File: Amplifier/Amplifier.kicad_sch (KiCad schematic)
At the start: 55 parts, among them J7 Conn_01x14_MountingPin, Q3 2N7002, U13 AD40xxBRMZ, U14 LP5907MFX-1.8, U16 LTC6268xS8, U2 LMP7721, U6 ADA4940-1xCP

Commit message: commiting pcb changes
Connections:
- net VDDA: now also J7.10 (Pin_10); no longer J7.12 (Pin_12)
- net VSSA: now also J7.12 (Pin_12); no longer J7.10 (Pin_10)
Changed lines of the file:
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@@
 	(symbol
 		(lib_id "power:VDDA")
-		(at 49.53 111.76 90)
+		(at 49.53 106.68 90)
 		(mirror x)
 		(unit 1)
@@
 		(fields_autoplaced yes)
 		(property "Reference" "#PWR024"
-			(at 53.34 111.76 0)
+			(at 53.34 106.68 0)
 			(hide yes)
 			(show_name no)
@@
 		)
 		(property "Value" "VDDA"
-			(at 46.355 111.7601 90)
+			(at 46.355 106.6801 90)
 			(show_name no)
 			(do_not_autoplace no)
@@
 		)
 		(property "Footprint" ""
-			(at 49.53 111.76 0)
+			(at 49.53 106.68 0)
 			(hide yes)
 			(show_name no)
@@
 		)
 		(property "Datasheet" ""
-			(at 49.53 111.76 0)
+			(at 49.53 106.68 0)
 			(hide yes)
 			(show_name no)
@@
 		)
 		(property "Description" "Power symbol creates a global label with name \"VDDA\""
-			(at 49.53 111.76 0)
+			(at 49.53 106.68 0)
 			(hide yes)
 			(show_name no)
@@
 	(symbol
 		(lib_id "power:VSSA")
-		(at 49.53 106.68 90)
+		(at 49.53 111.76 90)
 		(unit 1)
 		(body_style 1)
@@
 		(dnp no)
 		(property "Reference" "#PWR022"
-			(at 53.34 106.68 0)
+			(at 53.34 111.76 0)
 			(hide yes)
 			(show_name no)
@@
 		)
 		(property "Value" "VSSA"
-			(at 46.228 106.68 90)
+			(at 46.228 111.76 90)
 			(show_name no)
 			(do_not_autoplace no)
@@
 		)
 		(property "Footprint" ""
-			(at 49.53 106.68 0)
+			(at 49.53 111.76 0)
 			(hide yes)
 			(show_name no)
@@
 		)
 		(property "Datasheet" ""
-			(at 49.53 106.68 0)
+			(at 49.53 111.76 0)
 			(hide yes)
 			(show_name no)
@@
 		)
 		(property "Description" "Power symbol creates a global label with name \"VSSA\""
-			(at 49.53 106.68 0)
-			(hide yes)
-			(show_name no)
+			(at 49.53 111.76 0)
+			(hide yes)
+			(show_name no)

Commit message: chore: prepare repository and documentation for open-source release
- Removed internal .agents scaffolding and updated .gitignore
- Added CONTRIBUTING.md with CAD, PCB, firmware, and PR guidelines
- Added CODE_OF_CONDUCT.md (Contributor Covenant v2.1)
- Added SECURITY.md with hardware safety and vulnerability disclosure policies
- Added CITATION.cff for academic and scientific publications
- Added Pump_firmware/README.md for STM32G431 subsystem
- Expanded BOM.md with mechanical, fluidic, PCB, and active electronics
- Updated README.md test badges, architecture, and documentation index
- Cleared hardcoded absolute developer paths in export_manager.py and KiCad files
- Fixed formatting in install.sh and metadata in package.json
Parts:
- removed NT5: NetTie_2, NetTie:NetTie-2_SMD_Pad0.5mm, symbol Device:NetTie_2
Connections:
- net Signal_AMP: no longer C9.1, R3.1, R45.1, U16.6
- new net Signal_Return: C9.1, R3.1, R45.1, U16.6
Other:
- moved on the sheet: C9, R5

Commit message: feat: Add Path 2 wideband TIA channel for 200nm pores
Co-authored-by: google-labs-jules[bot] <161369871+google-labs-jules[bot]@users.noreply.github.com>
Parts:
- J_POGO1: value PogoPin_SpringHeader_6Pin_Array -> PogoPin_SpringHeader_12Pin_Distributed; footprint footprints:PogoPin_Target_6Pin_Distributed -> footprints:PogoPin_SpringHeader_12Pin_Distributed; symbol MR1:PogoPin_SpringHeader_6Pin_Array -> MR1:PogoPin_SpringHeader_12Pin_Distributed
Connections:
- net >PORE_AMP: no longer J_POGO1.6 (WE_POS)
- net CE_GNDA: no longer J_POGO1.1 (CE_GNDA)
- net GNDA: no longer J_POGO1.3 (GNDA)
- net RE_TRANS: no longer J_POGO1.2 (RE_TRANS)
- net R_WEEP_LIM: no longer J_POGO1.5 (WS_CIS)
- net WS_CIS: no longer J_POGO1.4 (WEEP_SENSE)
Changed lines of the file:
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@@
 	)
 	(symbol
-		(lib_id "MR1:PogoPin_SpringHeader_6Pin_Array")
+		(lib_id "MR1:PogoPin_SpringHeader_12Pin_Distributed")
 		(at 46.99 30.48 0)
 		(unit 1)
@@
 			)
 		)
-		(property "Value" "PogoPin_SpringHeader_6Pin_Array"
+		(property "Value" "PogoPin_SpringHeader_12Pin_Distributed"
 			(at 58.42 31.7499 0)
 			(show_name no)
@@
 			)
 		)
-		(property "Footprint" "footprints:PogoPin_Target_6Pin_Distributed"
+		(property "Footprint" "footprints:PogoPin_SpringHeader_12Pin_Distributed"
 			(at 46.99 30.48 0)
 			(hide yes)
@@
 		(pin "6"
 		)
+		(pin "7")
+		(pin "8")
+		(pin "9")
+		(pin "10")
+		(pin "11")
+		(pin "12")
 		(instances
 			(project "Amplifier"
@@
 	(embedded_fonts no)
 )
+	(label "WS_CIS_WIDE" (at 40.64 125.0 180) (effects (font (size 1.27 1.27))))
+	(label "GUARD_WIDE" (at 40.64 130.0 180) (effects (font (size 1.27 1.27))))
+	(symbol (lib_id "Amplifier_Operational:OPA192") (at 100.0 125.0 0) (unit 1)
+		(property "Reference" "U17" (at 101.6 120.0 0) (effects (font (size 1.27 1.27))))
+		(property "Value" "OPA192" (at 101.6 122.5 0) (effects (font (size 1.27 1.27))))
+	)
+	(symbol (lib_id "Device:R") (at 100.0 115.0 90) (unit 1)
+		(property "Reference" "Rf2" (at 100.0 112.0 0) (effects (font (size 1.27 1.27))))
+		(property "Value" "100k" (at 100.0 118.0 0) (effects (font (size 1.27 1.27))))
+	)
+	(symbol (lib_id "Device:C") (at 100.0 110.0 90) (unit 1)
+		(property "Reference" "Cf2" (at 100.0 107.0 0) (effects (font (size 1.27 1.27))))
+		(property "Value" "15pF" (at 100.0 109.0 0) (effects (font (size 1.27 1.27))))
+	)
+	(wire (pts (xy 40.64 125.0) (xy 90.0 125.0)) (stroke (width 0) (type default)))
+	(wire (pts (xy 90.0 125.0) (xy 90.0 115.0)) (stroke (width 0) (type default)))
+	(wire (pts (xy 90.0 115.0) (xy 95.0 115.0)) (stroke (width 0) (type default)))
+	(wire (pts (xy 90.0 115.0) (xy 90.0 110.0)) (stroke (width 0) (type default)))
+	(wire (pts (xy 90.0 110.0) (xy 95.0 110.0)) (stroke (width 0) (type default)))
+	(wire (pts (xy 105.0 115.0) (xy 110.0 115.0)) (stroke (width 0) (type default)))
+	(wire (pts (xy 105.0 110.0) (xy 110.0 110.0)) (stroke (width 0) (type default)))
+	(wire (pts (xy 110.0 115.0) (xy 110.0 125.0)) (stroke (width 0) (type default)))
+	(wire (pts (xy 110.0 110.0) (xy 110.0 115.0)) (stroke (width 0) (type default)))
+	(wire (pts (xy 110.0 125.0) (xy 120.0 125.0)) (stroke (width 0) (type default)))
+	(label "Path2_OUT" (at 120.0 125.0 0) (effects (font (size 1.27 1.27))))

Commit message: lots of refinements.
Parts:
- removed J_POGO1: PogoPin_SpringHeader_12Pin_Distributed, footprints:PogoPin_SpringHeader_12Pin_Distributed, symbol MR1:PogoPin_SpringHeader_12Pin_Distributed
- added C14: 100nF, Capacitor_SMD:C_0805_2012Metric, symbol Device:C
- added C3: 15pF, Capacitor_SMD:C_0402_1005Metric, symbol Device:C
- added C34: 100nF, Capacitor_SMD:C_0402_1005Metric, symbol Device:C
- added FB1, FB2: HZ0402A152R-10, Inductor_SMD:L_0402_1005Metric, symbol Device:FerriteBead_Small
- added J_POGO2: PogoPin_SpringHeader_12Pin_Distributed, footprints:PogoPin_SpringHeader_12Pin_Distributed, symbol MR1:PogoPin_SpringHeader_12Pin_Distributed
- added NT6: NetTie_2, NetTie:NetTie-2_SMD_Pad0.5mm, symbol Device:NetTie_2
- added R10: 100k, Resistor_SMD:R_0402_1005Metric, symbol Device:R
- added R32, R33: 49.9, Resistor_SMD:R_0402_1005Metric, symbol Device:R_Small_US
- added R9: 1K, Resistor_SMD:R_0402_1005Metric, symbol Device:R
- added U5: OPA192IDR, footprints:SOIC-8_3.9x4.9mm_P1.27mm, symbol MR1:OPA192IDR
- R1: value 1M -> 1G
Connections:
- net +3V3: now also FB1.1, FB2.1; no longer C33.1, U13.10 (VIO), U14.1 (IN)
- net >PORE_AMP: now also J_POGO2.3 (>PORE)
- net CE_GNDA: now also J_POGO2.1 (CE_GNDA)
- net GND: no longer C11.2, J7.4 (Pin_4), U14.2 (GND)
- net GNDA: now also C11.2, U14.2 (GND), C14.2, C34.2, J_POGO2.11 (GNDA), J_POGO2.4 (GNDA), J_POGO2.8 (GNDA)
- net GUARD: now also J_POGO2.5 (GUARD), J_POGO2.7 (GUARD)
- net RE_TRANS: now also J_POGO2.2 (RE_TRANS), R9.2
- net R_WEEP_LIM: now also J_POGO2.12 (WEEP_SENSE)
- net Signal_Return: now also R32.2
- net VDDA: now also U5.7 (V+)
- net VSSA: now also U5.4 (V-)
- net Vbias: now also C14.1, NT6.2, R9.1, U5.3 (+)
- net WS_CIS: now also J_POGO2.6 (WS_CIS)
- new net: C3.1, R10.1, R32.1, U5.6
- new net: C34.1, FB2.2, U14.1 (IN)
- new net: J7.4 (Pin_4), R33.2
- new net +3.3VA: C33.1, FB1.2, U13.10 (VIO)
- new net GUARD_WIDE: J_POGO2.9 (GUARD_WIDE), NT6.1, U5.1 (NC), U5.5 (NC), U5.8 (NC)
- new net ROUTE_SEL: R33.1
- new net WS_CIS_WIDE: C3.2, J_POGO2.10 (WS_CIS_WIDE), R10.2, U5.2 (-)

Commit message: there's issues with the constrictic iterposer mating pad showing up
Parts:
- removed NT6: NetTie_2, NetTie:NetTie-2_SMD_Pad0.5mm, symbol Device:NetTie_2
- added C40, C42: 100nF, Capacitor_SMD:C_0402_1005Metric, symbol Device:C
- added J_PAD1: Concentric_Interposer_Mating_Pad, footprints:Concentric_Interposer_Mating_Pad, symbol MR1:Concentric_Interposer_Mating_Pad
- added U17: ADG1219BRMZ, footprints:MSOP-8_3x3mm_P0.65mm, symbol MR1:ADG1219BRMZ
- added unit 2 of U5
- U5: value OPA192IDR -> OPA2192IDR; symbol MR1:OPA192IDR -> MR1:OPA2192IDR; MPN OPA192IDR -> OPA2192IDR; Mouser PN 595-OPA192IDR -> 595-OPA2192IDR
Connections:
- net +3V3: now also U17.1 (EN)
- net >PORE_AMP: now also J_PAD1.1 (SIG)
- net GNDA: now also C40.2, C42.2, U17.3 (GND)
- net GUARD: now also J_PAD1.2 (GUARD)
- net GUARD_WIDE: now also U5.6 (-), U5.7; no longer U5.1 (NC), U5.5 (NC), U5.8 (NC)
- net ROUTE_SEL: now also U17.8 (IN)
- net Signal_Return: now also U17.6 (D); no longer C9.1, R3.1, R32.2, U16.6
- net VDDA: now also U5.8 (V+), C40.1, U17.2 (VDD); no longer U5.7 (V+)
- net VSSA: now also C42.1, U17.4 (VSS)
- net Vbias: now also U5.5 (+)
- net at C3.1, R10.1, R32.1: now also U5.1; no longer U5.6
- new net Route1_OUT: C9.1, R3.1, U16.6, U17.7 (SA)
- new net Route2_OUT: R32.2, U17.5 (SB)
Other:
- moved on the sheet: C1, C10, C11, C12, C14, C19, C20, C3, C34, C39, C6, C7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

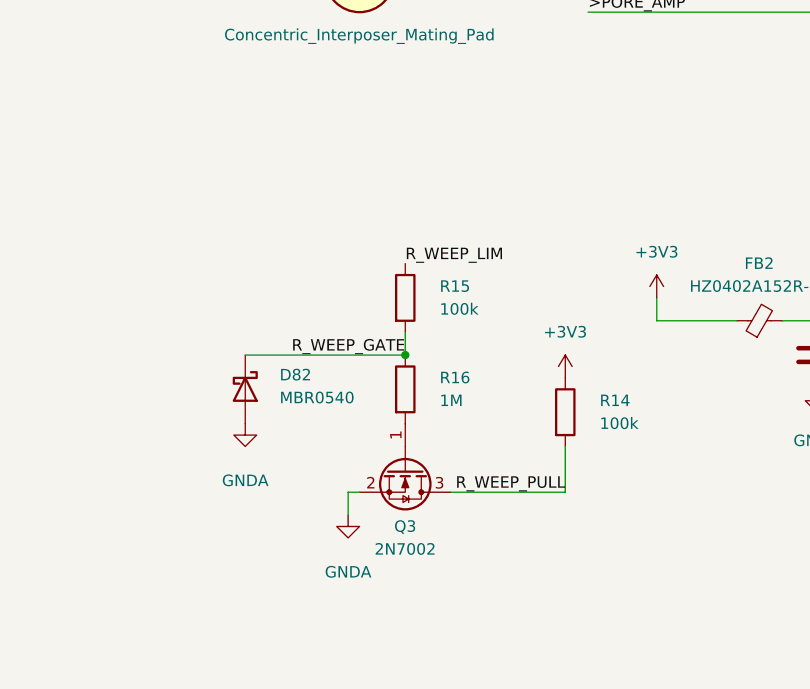
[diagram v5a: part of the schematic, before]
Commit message: added opamp_signal_conditioning and more refined repo
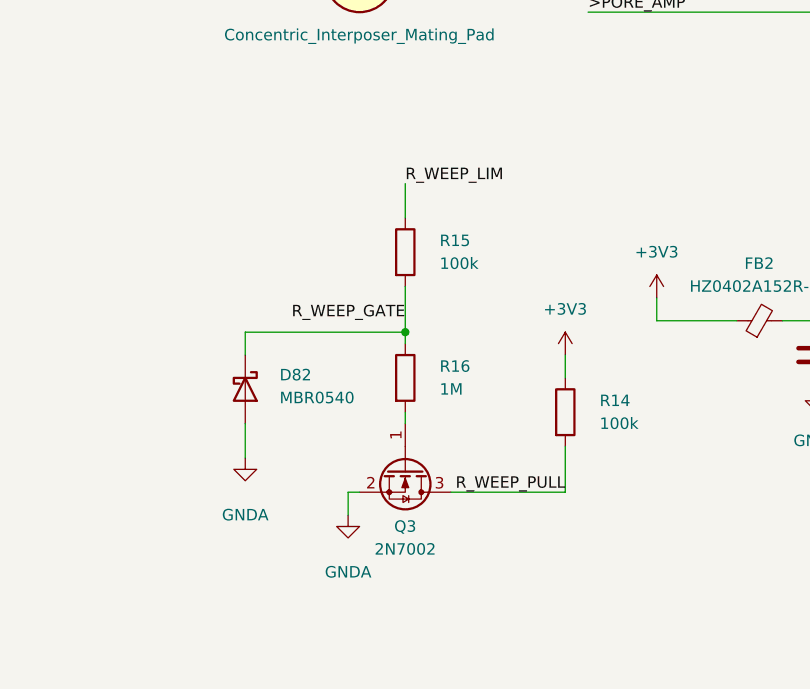
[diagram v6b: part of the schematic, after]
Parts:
- C1: LCSC (none) -> C161316
- C10, C12, C19, C31, C32, C33, C34, C39, C40, C42: LCSC (none) -> C15255
- C11: LCSC (none) -> C19702
- C14, C20, C6, C9: LCSC (none) -> C49678
- C29, C30: LCSC (none) -> C1548
- C3: LCSC (none) -> C33148
- C35: LCSC C1713 -> C1713
- C41: LCSC (none) -> C1523
- C7, C8: LCSC (none) -> C1525
- D82: LCSC (none) -> C5204747
- FB1, FB2: LCSC (none) -> C442654
- J7: LCSC (none) -> C2856818
- J_POGO2: LCSC (none) -> C49451500
- Q3: LCSC (none) -> C8545
- R1: LCSC (none) -> HVC0805T1007JET
- R10, R14, R15: LCSC (none) -> C60491
- R16: LCSC (none) -> C25488
- R27, R41: LCSC (none) -> C25078
- R28, R29, R30, R31, R32, R33: LCSC (none) -> C4074199
- R3, R5: LCSC (none) -> C17513
- R4: LCSC (none) -> C25097
- R43, R44, R45, R46: LCSC (none) -> C25132
- R6, R9: LCSC (none) -> C25149
- R8: LCSC (none) -> C17408
- U13: LCSC (none) -> C539308
- U14: LCSC (none) -> C92498
- U16: LCSC (none) -> C689169
- U17: LCSC (none) -> C206796
- U5: LCSC (none) -> C110074
- U6: LCSC (none) -> C529241
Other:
- moved on the sheet: R15, R16

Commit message: adding new symbols
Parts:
- removed J_POGO2: PogoPin_SpringHeader_12Pin_Distributed, footprints:PogoPin_SpringHeader_12Pin_Distributed, symbol MR1:PogoPin_SpringHeader_12Pin_Distributed
- added J_POGO1: PogoPin_SpringHeader_6Pin_Cis, footprints:PogoPin_SpringHeader_6Pin_Cis, symbol MR1:PogoPin_SpringHeader_6Pin_Cis
- added J_POGO2: PogoPin_SpringHeader_6Pin_Trans, footprints:PogoPin_SpringHeader_6Pin_Trans, symbol MR1:PogoPin_SpringHeader_6Pin_Trans
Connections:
- net >PORE_AMP: now also J_POGO1.2 (>PORE_AMP)
- net CE_GNDA: now also J_POGO2.1 (CE_GNDA)
- net GNDA: now also J_POGO1.1 (GNDA), J_POGO1.3 (GNDA), J_POGO1.5 (GNDA)
- net GUARD: now also J_POGO1.4 (GUARD), J_POGO2.5 (GUARD)
- net GUARD_WIDE: now also J_POGO2.3 (GUARD_WIDE)
- net RE_TRANS: now also J_POGO2.2 (RE_TRANS)
- net R_WEEP_LIM: now also J_POGO1.6 (WEEP_SENSE)
- net WS_CIS: now also J_POGO2.6 (WS_CIS)
- net WS_CIS_WIDE: now also J_POGO2.4 (WS_CIS_WIDE)

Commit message: feat: implement distributed 2x6 pogo pin map ($36mm span) across Bank A and Bank B and resolve merge conflicts
Co-authored-by: google-labs-jules[bot] <161369871+google-labs-jules[bot]@users.noreply.github.com>
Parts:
- removed J_PAD1: Concentric_Interposer_Mating_Pad, footprints:Concentric_Interposer_Mating_Pad, symbol MR1:Concentric_Interposer_Mating_Pad
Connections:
- net >PORE_AMP: now also J_POGO2.3 (>PORE_AMP); no longer J_POGO1.2 (>PORE_AMP)
- net GNDA: now also J_POGO1.4 (GNDA), J_POGO2.4 (GNDA), J_POGO2.5 (GNDA_WEEP); no longer J_POGO1.1 (GNDA), J_POGO1.3 (GNDA), J_POGO1.5 (GNDA)
- net GUARD: now also J_POGO1.1 (GUARD_1), J_POGO1.3 (GUARD_2); no longer J_POGO1.4 (GUARD), J_POGO2.5 (GUARD)
- net GUARD_WIDE: now also J_POGO1.6 (GUARD_WIDE); no longer J_POGO2.3 (GUARD_WIDE)
- net R_WEEP_LIM: now also J_POGO2.6 (WEEP_SENSE); no longer J_POGO1.6 (WEEP_SENSE)
- net WS_CIS: now also J_POGO1.2 (WS_CIS); no longer J_POGO2.6 (WS_CIS)
- net WS_CIS_WIDE: now also J_POGO1.5 (WS_CIS_WIDE); no longer J_POGO2.4 (WS_CIS_WIDE)
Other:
- note removed: "Add precision low noise ADC"
- note removed: "Look at Insturmentation amplifiers"
- note removed: "TODO: update ADC with correct library part and footprint add voltage reference,"
- moved on the sheet: H1, H2, H3, H4
